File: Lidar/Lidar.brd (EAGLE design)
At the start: 100 x 80 mm, 4 parts

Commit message: board schematic
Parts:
- moved ESP32 15.3 mm to (61.0, 39.4), turned to 180 degrees
- moved CONN-LIDAR 5.24 mm to (58.4, 73.7), turned to 180 degrees
- moved ALIM 1.80 mm to (12.7, 72.4)
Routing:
- net VCC: track 0.00 -> 106.2 mm
- net GND: track 0.00 -> 87.2 mm
- net RX: track 0.00 -> 50.1 mm
- net MOTORCTL: track 0.00 -> 35.9 mm
- net TX: track 0.00 -> 29.3 mm, vias 0 -> 1
- net V-: track 0.00 -> 12.5 mm
- net V+: track 0.00 -> 11.6 mm
- added copper zone on layer 16, net GNDPLATE
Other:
- board text added: "GND"
- board text added: "MCTL"
- board text added: "RX"
- board text added: "TX"
- board text added: "VCC"
- board text added: "Vin+"
- board text added: "Vin-"
- board text added: "Vout+"

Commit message: re-route everything
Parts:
- moved CONN-LIDAR 1.00 mm to (58.4, 74.7)
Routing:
- net VCC: track 106.2 -> 130.6 mm
- net RX: track 50.1 -> 31.8 mm
- net GND: track 87.2 -> 97.0 mm
- net MOTORCTL: track 35.9 -> 38.4 mm
- net TX: track 29.3 -> 30.3 mm, vias 1 -> 0
- added copper zone on layer 16, net GND
- removed copper zone on layer 16, net GNDPLATE

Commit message: (re-)use the VCC pin to avoid 90° routes
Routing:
- net VCC: track 130.6 -> 128.6 mm
- net GND: track 97.0 -> 98.6 mm
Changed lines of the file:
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@@
 <drawing>
 <settings>
-<setting alwaysvectorfont="yes"/>
+<setting alwaysvectorfont="no"/>
 <setting verticaltext="up"/>
 </settings>
@@
 <wire x1="48.97543125" y1="76.3872" x2="46.3872" y2="76.3872" width="1.27" layer="16"/>
 <wire x1="46.3872" y1="76.3872" x2="42" y2="72" width="1.27" layer="16"/>
-<wire x1="42" y1="72" x2="42" y2="36.92" width="1.27" layer="16"/>
-<wire x1="42" y1="36.92" x2="42" y2="25.87" width="1.27" layer="16"/>
+<wire x1="42" y1="72" x2="42" y2="25.87" width="1.27" layer="16"/>
 <wire x1="42" y1="25.87" x2="48.26" y2="19.61" width="1.27" layer="16"/>
-<wire x1="20.32" y1="15.24" x2="42" y2="36.92" width="1.27" layer="16"/>
 <polygon width="1.27" layer="16">
 <vertex x="0" y="80"/>
@@
 <vertex x="0" y="0"/>
 </polygon>
+<wire x1="40.89" y1="12.24" x2="48.26" y2="19.61" width="1.27" layer="16"/>
+<wire x1="20.32" y1="15.24" x2="23.32" y2="12.24" width="1.27" layer="16"/>
+<wire x1="40.89" y1="12.24" x2="23.32" y2="12.24" width="1.27" layer="16"/>
 </signal>
 <signal name="VCC">
@@
 <contactref element="TRACO" pad="4"/>
 <contactref element="ESP32" pad="J2-19"/>
-<wire x1="58.42" y1="74.66" x2="62.04" y2="71.04" width="1.27" layer="16"/>
-<wire x1="62.04" y1="71.04" x2="67.75" y2="65.33" width="1.27" layer="16"/>
-<wire x1="67.75" y1="65.33" x2="73.66" y2="65.33" width="1.27" layer="16"/>
-<wire x1="10.16" y1="15.24" x2="17.4" y2="8" width="1.27" layer="16"/>
-<wire x1="17.4" y1="8" x2="51" y2="8" width="1.27" layer="16"/>
-<wire x1="51" y1="8" x2="62.04" y2="19.04" width="1.27" layer="16"/>
-<wire x1="62.04" y1="19.04" x2="62.04" y2="71.04" width="1.27" layer="16"/>
+<wire x1="10.16" y1="15.24" x2="20.4" y2="5" width="1.27" layer="16"/>
+<wire x1="20.4" y1="5" x2="42" y2="5" width="1.27" layer="16"/>
+<wire x1="73.66" y1="65.33" x2="66" y2="57.67" width="1.27" layer="16"/>
+<wire x1="66" y1="29" x2="66" y2="57.67" width="1.27" layer="16"/>
+<wire x1="42" y1="5" x2="66" y2="29" width="1.27" layer="16"/>
+<wire x1="58.42" y1="74.66" x2="64.33" y2="74.66" width="1.27" layer="16"/>
+<wire x1="64.33" y1="74.66" x2="73.66" y2="65.33" width="1.27" layer="16"/>
 </signal>
 <signal name="RX">

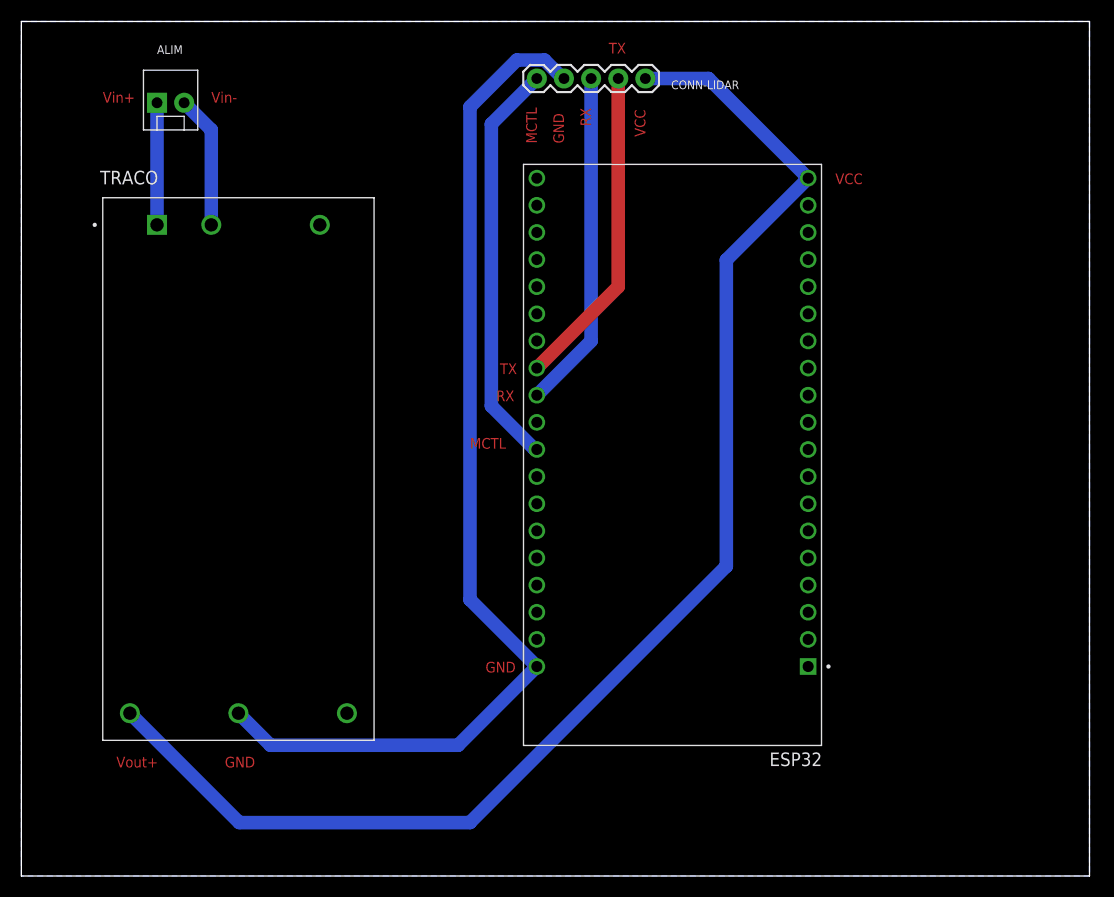
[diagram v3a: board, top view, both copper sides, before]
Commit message: add(lidar): POWER LED + reduce the board size
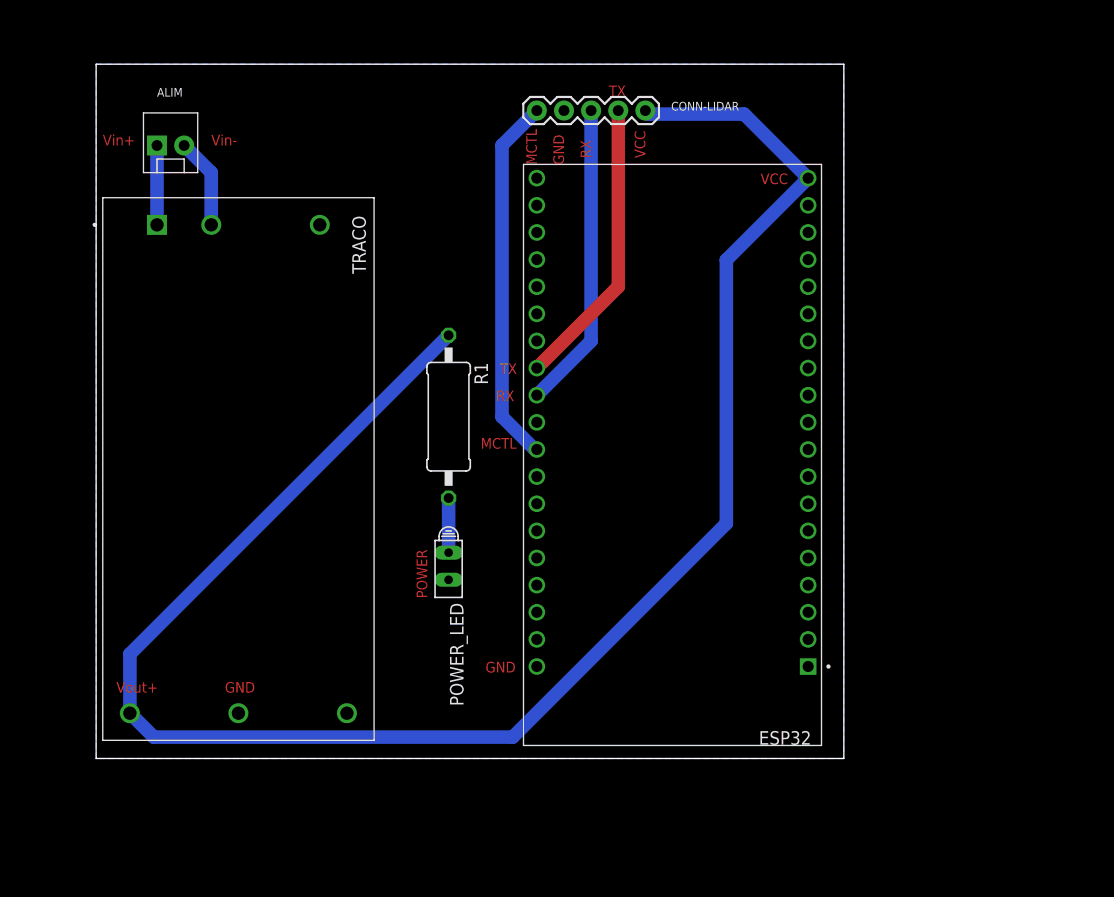
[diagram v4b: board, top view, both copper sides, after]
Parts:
- added POWER_LED: HLMP6, display-hp:HLMP6
- added R1: 300Ohm, rcl:0411/15
- moved ALIM 4.00 mm to (12.7, 68.4)
- moved CONN-LIDAR 3.00 mm to (58.4, 71.7)
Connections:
- new net N$1: POWER_LED.A, R1.2
- net GND: now also POWER_LED.K
- net VCC: now also R1.1
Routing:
- net GND: track 98.6 -> 0.00 mm
- net VCC: track 128.6 -> 166.2 mm
- net N$1: track 0.00 -> 5.11 mm
- net V-: track 12.5 -> 8.48 mm
- net V+: track 11.4 -> 7.43 mm
- net MOTORCTL: track 38.4 -> 34.5 mm
- net TX: track 30.3 -> 27.3 mm
- net RX: track 31.8 -> 28.8 mm
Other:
- board size 100 x 80 mm -> 70 x 65 mm
- board text added: "POWER"
